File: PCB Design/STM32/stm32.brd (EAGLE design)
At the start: 71.1 x 84.3 mm, 68 parts, among them IC1 NCP1117ST50T3G, Q1 ABM3B-8.000MHZ-10-1UT, T5 BC847, T6 BC847, T7 BC847, T8 BC847, U1 STM32F103RET6, U2 MCP1700T-3302E/TT, U3 MCP1700T-3302E/TT, U4 MPU-6050, U5 TB6612FNG, X1 22-23-2031

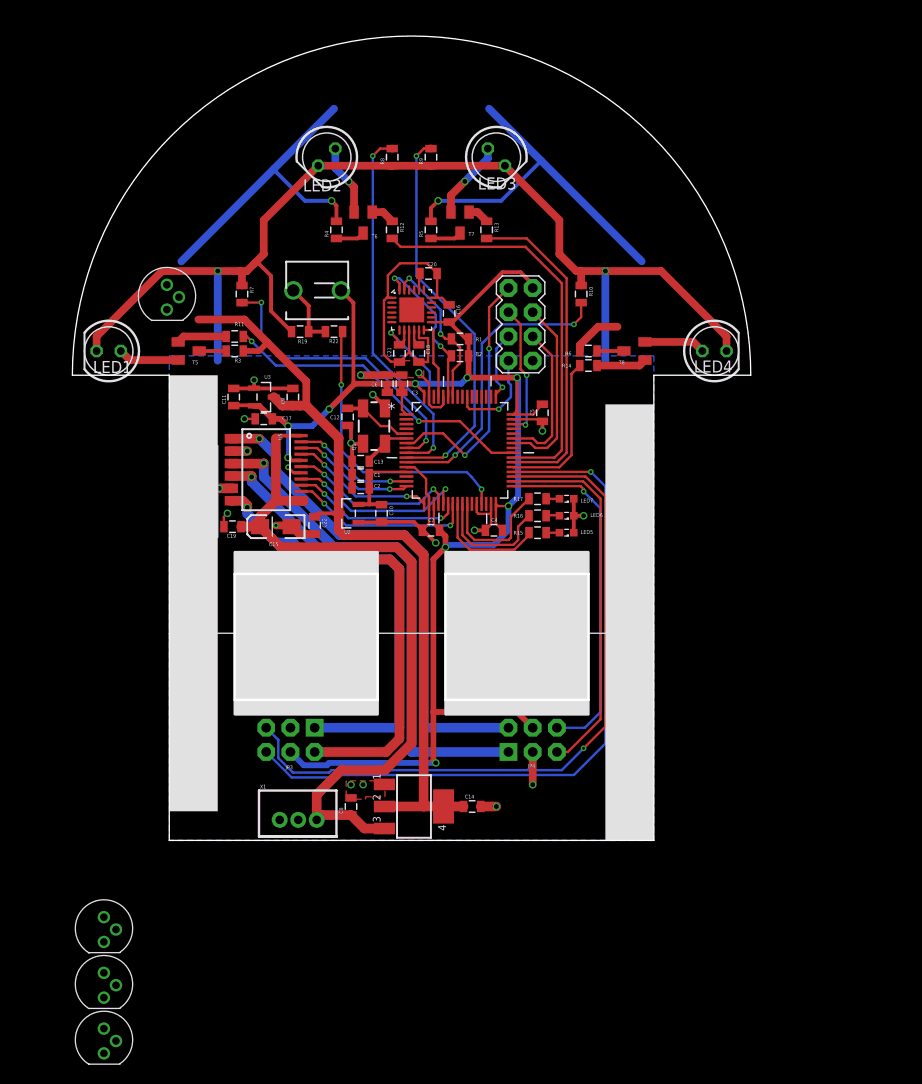
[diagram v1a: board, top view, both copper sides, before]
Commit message: updated power to phototransistors and encoders
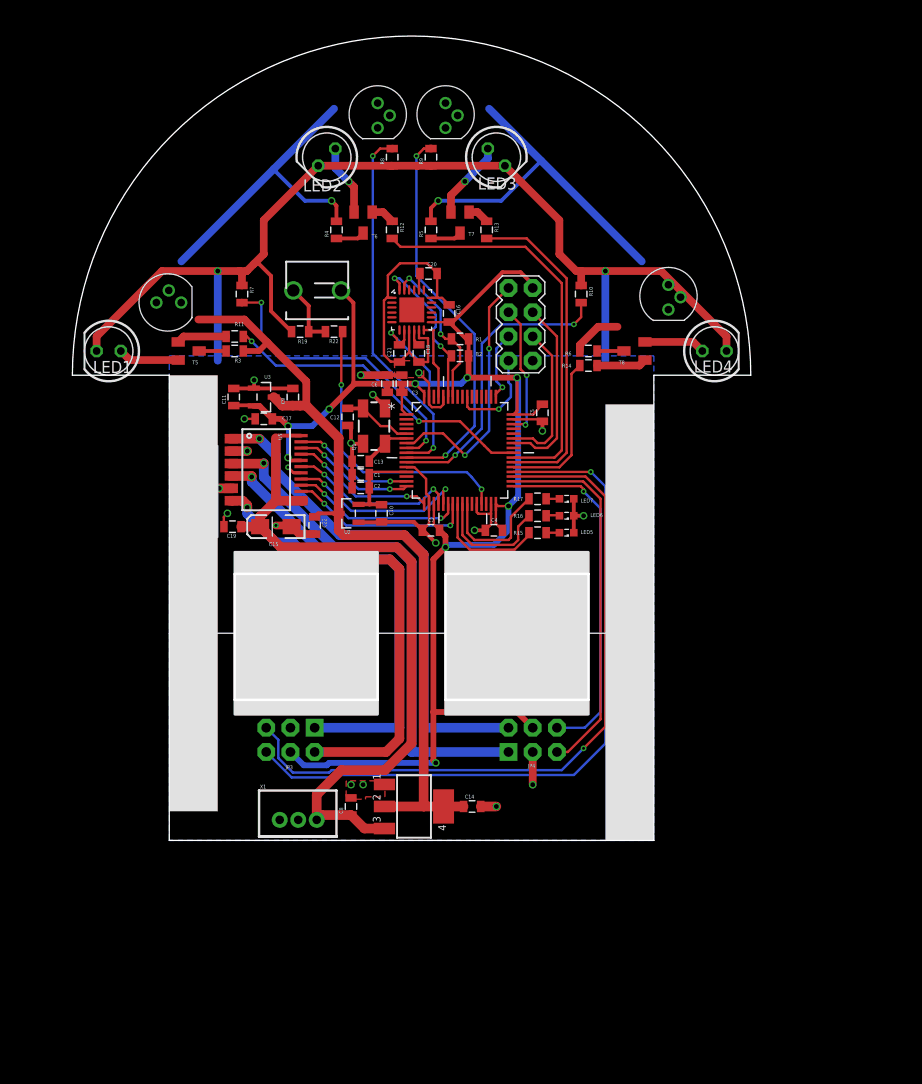
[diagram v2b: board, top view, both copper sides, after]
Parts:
- moved U$4 98.0 mm to (41.4, 79.0)
- moved U$5 97.9 mm to (64.8, 59.9)
- moved U$3 90.0 mm to (34.3, 79.0)
- moved U$2 0.76 mm to (12.2, 59.2), turned to 90 degrees
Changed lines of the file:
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@@
 <setting verticaltext="up"/>
 </settings>
-<grid distance="10" unitdist="mil" unit="mil" style="lines" multiple="1" display="no" altdistance="0.025" altunitdist="inch" altunit="mil"/>
+<grid distance="0.01" unitdist="mm" unit="mm" style="lines" multiple="1" display="no" altdistance="0.01" altunitdist="mm" altunit="mm"/>
 <layers>
 <layer number="1" name="Top" color="4" fill="1" visible="yes" active="yes"/>
@@
 <layer number="16" name="Bottom" color="1" fill="1" visible="yes" active="yes"/>
 <layer number="17" name="Pads" color="2" fill="1" visible="yes" active="yes"/>
-<layer number="18" name="Vias" color="2" fill="1" visible="yes" active="yes"/>
-<layer number="19" name="Unrouted" color="6" fill="1" visible="yes" active="yes"/>
+<layer number="18" name="Vias" color="2" fill="1" visible="no" active="yes"/>
+<layer number="19" name="Unrouted" color="6" fill="1" visible="no" active="yes"/>
 <layer number="20" name="Dimension" color="15" fill="1" visible="yes" active="yes"/>
 <layer number="21" name="tPlace" color="7" fill="1" visible="yes" active="yes"/>
-<layer number="22" name="bPlace" color="7" fill="1" visible="yes" active="yes"/>
-<layer number="23" name="tOrigins" color="15" fill="1" visible="yes" active="yes"/>
-<layer number="24" name="bOrigins" color="15" fill="1" visible="yes" active="yes"/>
-<layer number="25" name="tNames" color="7" fill="1" visible="yes" active="yes"/>
-<layer number="26" name="bNames" color="7" fill="1" visible="yes" active="yes"/>
+<layer number="22" name="bPlace" color="7" fill="1" visible="no" active="yes"/>
+<layer number="23" name="tOrigins" color="15" fill="1" visible="no" active="yes"/>
+<layer number="24" name="bOrigins" color="15" fill="1" visible="no" active="yes"/>
+<layer number="25" name="tNames" color="7" fill="1" visible="no" active="yes"/>
+<layer number="26" name="bNames" color="7" fill="1" visible="no" active="yes"/>
 <layer number="27" name="tValues" color="7" fill="1" visible="no" active="yes"/>
 <layer number="28" name="bValues" color="7" fill="1" visible="no" active="yes"/>
@@
 </polygon>
 <wire x1="12.446" y1="24.511" x2="63.246" y2="24.511" width="0" layer="21"/>
+<dimension x1="2.286" y1="51.562" x2="73.406" y2="51.562" x3="37.846" y3="63.51" textsize="1.778" layer="21"/>
+<dimension x1="37.846" y1="51.562" x2="37.80875" y2="87.12198125" x3="37.827375" y3="69.341990625" textsize="1.778" layer="21" dtype="radius"/>
+<dimension x1="37.66" y1="51.49" x2="37.3682375" y2="1.9508625" x3="37.51411875" y3="26.720428125" textsize="1.778" layer="21" dtype="radius"/>
+<dimension x1="73.406" y1="51.562" x2="63.246190625" y2="51.62328125" x3="68.326096875" y3="51.592640625" textsize="1.778" layer="21" dtype="radius"/>
+<dimension x1="17.526" y1="5.842" x2="12.446" y2="5.842" x3="14.986" y3="5.86" textsize="1.778" layer="21"/>
 </plain>
 <attributes>
@@
 <attribute name="VALUE" x="64.389" y="52.197" size="1.27" layer="27" rot="R90"/>
 </element>
-<element name="U$2" library="phototransistor" package="PHTRST" value="PHTRST" x="12.192" y="59.944"/>
-<element name="U$3" library="phototransistor" package="PHTRST" value="PHTRST" x="5.588" y="-6.35"/>
-<element name="U$4" library="phototransistor" package="PHTRST" value="PHTRST" x="5.588" y="-12.192"/>
-<element name="U$5" library="phototransistor" package="PHTRST" value="PHTRST" x="5.588" y="-18.034"/>
+<element name="U$2" library="phototransistor" package="PHTRST" value="PHTRST" x="12.192" y="59.182" rot="R90"/>
+<element name="U$3" library="phototransistor" package="PHTRST" value="PHTRST" x="34.29" y="78.994"/>
+<element name="U$4" library="phototransistor" package="PHTRST" value="PHTRST" x="41.402" y="78.994"/>
+<element name="U$5" library="phototransistor" package="PHTRST" value="PHTRST" x="64.77" y="59.944"/>
 </elements>
 <signals>
@@
 <wire x1="22.098" y1="55.372" x2="22.098" y2="59.182" width="0.254" layer="16"/>
 <contactref element="U$2" pad="P$E"/>
-<wire x1="12.192" y1="58.444" x2="37.3126" y2="43.942" width="0" layer="19" extent="1-1"/>
+<wire x1="13.692" y1="59.182" x2="37.3126" y2="43.942" width="0" layer="19" extent="1-1"/>
 </signal>
 <signal name="IR_IN2">
@@
 <wire x1="34.544" y1="75.322" x2="35.814" y2="75.322" width="0.254" layer="1"/>
 <contactref element="U$3" pad="P$E"/>
-<wire x1="5.588" y1="-7.85" x2="37.3126" y2="43.434" width="0" layer="19" extent="1-1"/>
+<wire x1="34.29" y1="77.494" x2="37.3126" y2="43.434" width="0" layer="19" extent="1-1"/>
 </signal>
 <signal name="IR_IN3">
@@
 <wire x1="39.127" y1="75.322" x2="39.878" y2="75.322" width="0.254" layer="1"/>
 <contactref element="U$4" pad="P$E"/>
-<wire x1="5.588" y1="-13.692" x2="37.3126" y2="42.926" width="0" layer="19" extent="1-1"/>
+<wire x1="41.402" y1="77.494" x2="37.3126" y2="42.926" width="0" layer="19" extent="1-1"/>
 </signal>
 <signal name="IR_IN4">
@@
 <wire x1="41.6814" y1="42.4434" x2="37.3126" y2="42.4434" width="0.254" layer="1"/>
 <contactref element="U$5" pad="P$E"/>
-<wire x1="5.588" y1="-19.534" x2="37.3126" y2="42.4434" width="0" layer="19" extent="1-1"/>
+<wire x1="64.77" y1="58.444" x2="37.3126" y2="42.4434" width="0" layer="19" extent="1-1"/>
 </signal>
 <signal name="IR_OUT2">
@@
 <wire x1="29.972" y1="67.702" x2="39.878" y2="67.702" width="0" layer="19" extent="1-1"/>
 <wire x1="15.494" y1="57.404" x2="13.716" y2="63.5" width="0" layer="19" extent="1-16"/>
-<wire x1="13.462" y1="59.744" x2="35.0012" y2="6.35" width="0" layer="19" extent="1-1"/>
-<wire x1="6.858" y1="-6.55" x2="13.462" y2="59.744" width="0" layer="19" extent="1-1"/>
-<wire x1="6.858" y1="-12.392" x2="6.858" y2="-6.55" width="0" layer="19" extent="1-1"/>
-<wire x1="6.858" y1="-18.234" x2="6.858" y2="-12.392" width="0" layer="19" extent="1-1"/>
+<wire x1="12.392" y1="60.452" x2="35.0012" y2="6.35" width="0" layer="19" extent="1-1"/>
+<wire x1="35.56" y1="78.794" x2="12.392" y2="60.452" width="0" layer="19" extent="1-1"/>
+<wire x1="42.672" y1="78.794" x2="35.56" y2="78.794" width="0" layer="19" extent="1-1"/>
+<wire x1="66.04" y1="59.744" x2="42.672" y2="78.794" width="0" layer="19" extent="1-1"/>
 </signal>
 <signal name="N$1">

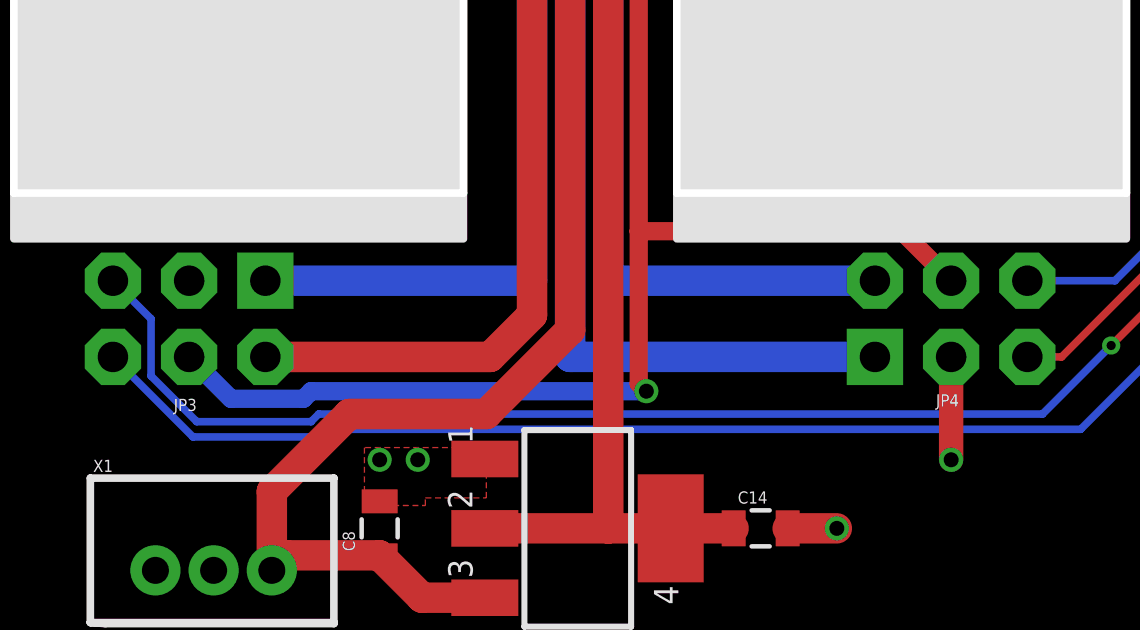
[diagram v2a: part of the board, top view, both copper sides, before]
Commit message: updated power to phototransistors and the encoders
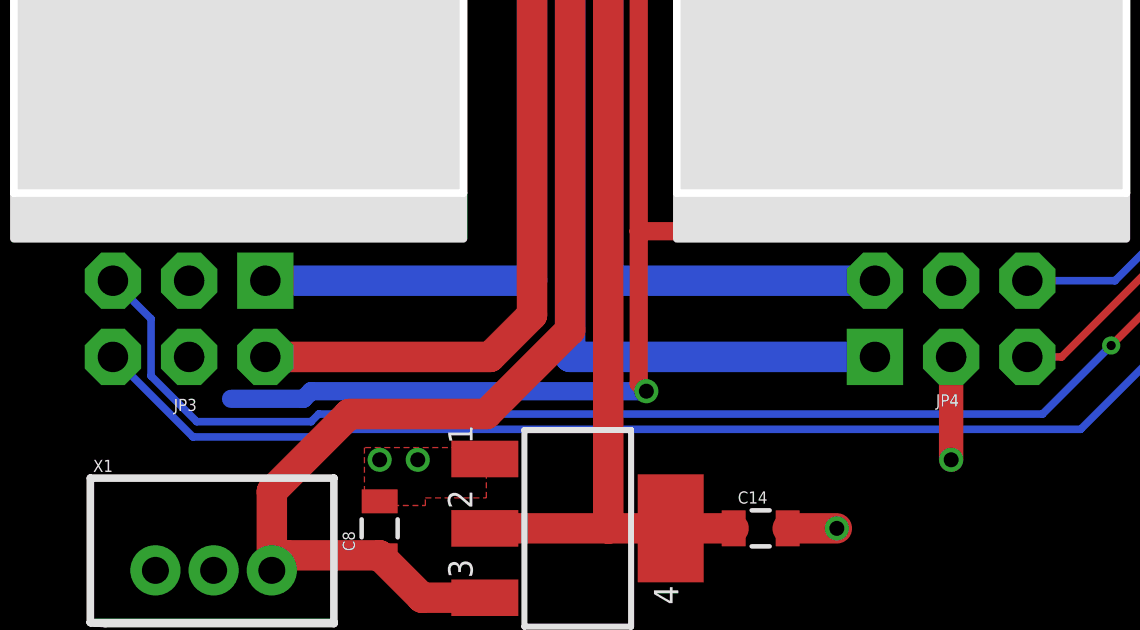
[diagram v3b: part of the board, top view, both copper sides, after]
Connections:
- net 5V: now also JP3.4, JP4.4; no longer U$2.P$C, U$3.P$C, U$4.P$C, U$5.P$C
- net VCC: now also U$2.P$C, U$3.P$C, U$4.P$C, U$5.P$C; no longer JP3.4, JP4.4
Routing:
- net VCC: track 176.4 -> 172.1 mm
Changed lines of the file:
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@@
 <contactref element="U3" pad="2"/>
 <contactref element="C21" pad="1"/>
-<contactref element="JP4" pad="4"/>
-<contactref element="JP3" pad="4"/>
 <contactref element="U5" pad="20"/>
 <contactref element="C17" pad="1"/>
@@
 <wire x1="30.452" y1="60.452" x2="31.75" y2="59.154" width="0.4064" layer="1"/>
 <wire x1="31.75" y1="59.154" x2="31.75" y2="50.8" width="0.4064" layer="1"/>
-<wire x1="50.546" y1="14.605" x2="48.895" y2="16.256" width="0.6096" layer="1"/>
 <wire x1="48.895" y1="16.256" x2="40.132" y2="16.256" width="0.6096" layer="1"/>
 <via x="40.386" y="10.922" extent="1-16" drill="0.5"/>
-<wire x1="26.543" y1="10.668" x2="25.146" y2="12.065" width="0.6096" layer="16"/>
 <wire x1="40.132" y1="16.256" x2="40.132" y2="11.176" width="0.6096" layer="1"/>
 <wire x1="40.132" y1="11.176" x2="40.386" y2="10.922" width="0.6096" layer="1"/>
@@
 <wire x1="49.022" y1="38.862" x2="48.006" y2="37.846" width="0.6096" layer="16"/>
 <wire x1="31.877" y1="50.673" x2="31.75" y2="50.8" width="0.4064" layer="1"/>
+<contactref element="U$2" pad="P$C"/>
+<contactref element="U$3" pad="P$C"/>
+<contactref element="U$4" pad="P$C"/>
+<contactref element="U$5" pad="P$C"/>
+<wire x1="50.546" y1="60.706" x2="66.04" y2="59.744" width="0" layer="19" extent="1-1"/>
+<wire x1="12.392" y1="60.452" x2="19.2024" y2="48.4124" width="0" layer="19" extent="1-1"/>
+<wire x1="42.672" y1="78.794" x2="47.371" y2="62.357" width="0" layer="19" extent="1-1"/>
+<wire x1="35.56" y1="78.794" x2="42.672" y2="78.794" width="0" layer="19" extent="1-1"/>
 </signal>
 <signal name="JTAG-TRST">
@@
 <wire x1="20.204" y1="54.102" x2="21.844" y2="54.102" width="0.6096" layer="1"/>
 <wire x1="21.844" y1="54.102" x2="22.733" y2="54.991" width="0.6096" layer="1"/>
-<contactref element="U$2" pad="P$C"/>
-<contactref element="U$3" pad="P$C"/>
-<contactref element="U$4" pad="P$C"/>
-<contactref element="U$5" pad="P$C"/>
+<contactref element="JP3" pad="4"/>
+<contactref element="JP4" pad="4"/>
 <wire x1="61.976" y1="63.5" x2="59.436" y2="56.642" width="0" layer="19" extent="1-16"/>
 <wire x1="29.972" y1="67.702" x2="39.878" y2="67.702" width="0" layer="19" extent="1-1"/>
 <wire x1="15.494" y1="57.404" x2="13.716" y2="63.5" width="0" layer="19" extent="1-16"/>
-<wire x1="12.392" y1="60.452" x2="35.0012" y2="6.35" width="0" layer="19" extent="1-1"/>
-<wire x1="35.56" y1="78.794" x2="12.392" y2="60.452" width="0" layer="19" extent="1-1"/>
-<wire x1="42.672" y1="78.794" x2="35.56" y2="78.794" width="0" layer="19" extent="1-1"/>
-<wire x1="66.04" y1="59.744" x2="42.672" y2="78.794" width="0" layer="19" extent="1-1"/>
+<wire x1="50.546" y1="14.605" x2="43.296" y2="6.35" width="0" layer="19" extent="1-1"/>
+<wire x1="25.146" y1="12.065" x2="35.0012" y2="6.35" width="0" layer="19" extent="1-1"/>
 </signal>
 <signal name="N$1">

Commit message: save
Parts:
- added R18, R20, R21, R23: (no value), SparkFun-Resistors:0805
- moved R1 7.18 mm to (50.0, 56.4)
- moved U$5 7.15 mm to (71.9, 59.2)
- moved LED3 7.15 mm to (53.8, 73.7)
- moved R10 7.15 mm to (62.7, 59.3)
- moved R13 7.15 mm to (52.8, 66.0)
- moved R14 7.15 mm to (63.5, 51.8)
- moved R5 7.15 mm to (47.0, 66.0)
- moved R6 7.15 mm to (63.5, 53.3)
- moved R9 7.15 mm to (47.0, 73.7)
- moved U$4 7.15 mm to (48.5, 78.2)
- moved LED4 7.15 mm to (76.7, 53.3)
- moved T8 7.15 mm to (68.3, 53.3)
- moved T7 7.15 mm to (50.0, 66.8)
- moved LED7 5.93 mm to (59.9, 39.6)
- moved C10 5.93 mm to (40.5, 38.1)
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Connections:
- new net N$20: R18.2, U1.33
- new net N$21: R20.2, U1.34
- new net N$29: R21.2, U1.35
- new net N$30: R23.2, U1.36
- net M1CA: now also R18.1; no longer U1.33
- net M1CB: now also R20.1; no longer U1.34
- net M2CA: now also R23.1; no longer U1.36
- net M2CB: now also R21.1; no longer U1.35
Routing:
- net BUTTON1: track 30.5 -> 18.0 mm, vias 2 -> 1
- net JTAG-TDO: track 10.2 -> 0.00 mm, vias 1 -> 0
- net GND: track 233.1 -> 241.9 mm
- net M2CA: track 75.3 -> 67.2 mm
- net VCC: track 172.1 -> 164.4 mm
- net M2CB: track 75.2 -> 67.7 mm
- net JTAG-TCK: track 7.40 -> 0.00 mm, vias 1 -> 0
- net M1CB: track 39.0 -> 31.7 mm
- net M1CA: track 36.8 -> 29.8 mm
- net I2C1_SDA: track 17.0 -> 23.2 mm
- net 5V: track 161.7 -> 156.3 mm
- net I2C1_SCL: track 16.7 -> 21.3 mm
- net N$31: track 6.74 -> 3.40 mm
- net N$10: track 1.75 -> 4.63 mm
- net INT: track 8.22 -> 11.0 mm
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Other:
- board size 71.1 x 84.3 mm -> 71.1 x 82.5 mm

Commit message: sleep
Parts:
- removed R18, R20, R21, R23: (no value), SparkFun-Resistors:0805
- moved U$5 2.90 mm to (69.1, 58.4), turned to 270 degrees
- moved R1 1.30 mm to (48.8, 56.1)
- moved C6 1.27 mm to (41.1, 51.7)
- moved LED7 1.02 mm to (59.9, 38.6)
- moved R17 1.02 mm to (56.9, 38.6)
- moved LED6 0.76 mm to (59.9, 37.1)
- moved R16 0.76 mm to (56.9, 37.1)
- moved U$2 0.51 mm to (16.8, 57.9)
- moved LED5 0.51 mm to (59.9, 35.6)
- moved R15 0.51 mm to (56.9, 35.6)
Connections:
- removed net N$20: R18.2, U1.33
- removed net N$21: R20.2, U1.34
- removed net N$29: R21.2, U1.35
- removed net N$30: R23.2, U1.36
- net M1CA: now also U1.33; no longer R18.1
- net M1CB: now also U1.34; no longer R20.1
- net M2CA: now also U1.36; no longer R23.1
- net M2CB: now also U1.35; no longer R21.1
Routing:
- net VCC: track 164.4 -> 79.1 mm, vias 10 -> 8
- net GND: track 241.9 -> 204.8 mm, vias 21 -> 19
- net JTAG-TMS: track 14.5 -> 2.90 mm, vias 2 -> 0
- net BUTTON1: track 18.0 -> 28.6 mm, vias 1 -> 2
- net I2C1_SDA: track 23.2 -> 15.8 mm
- net 5V: track 156.3 -> 150.0 mm
- net I2C1_SCL: track 21.3 -> 15.9 mm
- net N$9: track 3.40 -> 0.00 mm
- net INT: track 11.0 -> 7.63 mm
- net N$10: track 4.63 -> 1.75 mm
- net N$27: track 1.93 -> 0.00 mm
- net N$31: track 3.40 -> 1.76 mm
- net IR_OUT4: track 16.5 -> 15.1 mm
- net LED3: track 13.3 -> 12.0 mm
- net IR_IN2: track 38.5 -> 37.4 mm
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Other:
- outline, holes or cut-outs redrawn

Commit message: save
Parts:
- moved U$3 1.27 mm to (40.1, 78.2), turned to 315 degrees
- moved JP3 1.02 mm to (31.0, 13.3)
- moved JP4 1.02 mm to (56.4, 13.3)
- moved U$5 0.72 mm to (69.6, 57.9)
- moved U$2 0.72 mm to (17.3, 58.4), turned to 270 degrees
- moved U$4 0.25 mm to (48.5, 78.0), turned to 225 degrees
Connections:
- net JTAG-TCK: now also U$1.7; no longer U$1.5
- net JTAG-TDO: now also U$1.5; no longer U$1.7
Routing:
- net M1CA: track 29.8 -> 42.6 mm
- net M1CB: track 31.7 -> 44.3 mm
- net M2CA: track 67.2 -> 79.2 mm
- net M2CB: track 67.7 -> 79.5 mm
- net JTAG-TCK: track 0.00 -> 6.44 mm, vias 0 -> 1
- net VCC: track 79.1 -> 85.5 mm
- net N$31: track 1.76 -> 6.74 mm
- net GND: track 204.8 -> 208.0 mm
- net JTAG-TDO: track 0.00 -> 1.40 mm
- net M1-: track 54.3 -> 55.3 mm
- net M1+: track 55.5 -> 56.6 mm
- net M2+: track 48.6 -> 49.6 mm
- net IR_IN4: track 30.2 -> 31.0 mm
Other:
- board size 71.1 x 82.5 mm -> 81.3 x 81.1 mm

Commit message: save
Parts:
- moved R8 2.19 mm to (38.4, 72.8), turned to 0 degrees
- moved C14 2.06 mm to (52.1, 7.37)
- moved IC1 2.06 mm to (46.0, 7.37)
- moved X1 2.06 mm to (34.1, 7.37)
- moved C8 1.59 mm to (38.9, 6.91)
- moved R9 1.17 mm to (47.7, 72.7), turned to 180 degrees
- moved U$2 1.02 mm to (18.3, 58.4)
- moved U$3 1.02 mm to (39.1, 78.2)
- moved U$5 0.72 mm to (69.1, 58.4)
- moved U$4 0.36 mm to (48.3, 78.2)
- moved C5 0.25 mm to (57.4, 48.9)
- moved R4 0.25 mm to (34.3, 66.0)
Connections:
- removed net LED4: U1.27
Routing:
- net VCC: track 85.5 -> 193.8 mm, vias 8 -> 9
- net 5V: track 150.0 -> 100.0 mm
- net JTAG-TMS: track 2.90 -> 15.4 mm, vias 0 -> 2
- net JTAG-TDO: track 1.40 -> 13.7 mm, vias 0 -> 1
- net IR_IN1: track 31.6 -> 41.2 mm
- net GND: track 208.0 -> 217.0 mm, vias 19 -> 20
- net IR_IN3: track 39.5 -> 44.7 mm
- net IR_IN4: track 31.0 -> 35.8 mm
- net V_BATT: track 77.8 -> 76.0 mm
- net JTAG-TCK: track 6.44 -> 4.64 mm
- net N$9: track 0.00 -> 1.77 mm
- net IR_IN2: track 37.4 -> 39.0 mm
- net N$27: track 0.00 -> 1.40 mm

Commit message: final edition
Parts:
- moved R9 3.15 mm to (45.0, 74.3), turned to 0 degrees
- moved R10 2.54 mm to (65.3, 59.3)
- moved R8 2.30 mm to (40.1, 74.3), turned to 180 degrees
- moved C9 0.90 mm to (31.4, 51.2)
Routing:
- net GND: track 217.0 -> 93.6 mm, vias 20 -> 79
- net 5V: track 100.0 -> 170.1 mm, vias 2 -> 5
- net VCC: track 193.8 -> 211.1 mm
- net IR_IN3: track 44.7 -> 43.6 mm
